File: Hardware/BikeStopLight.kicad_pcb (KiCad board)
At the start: 2 copper layers, 63 parts, among them J1 ST-Link, J2 PWR, J3 BAT, J4 Conn_01x01, J5 Conn_01x01, J6 Conn_01x08, Q1 NTD4909N, U1 MCP1703A-3302_SOT23, U2 STM32L052K8Tx, U3 RFM95W-868S2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

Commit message: WIP - Routed
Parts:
- removed J3: BAT, Connector_PinHeader_2.54mm:PinHeader_1x02_P2.54mm_Vertical
- added R8: 0 Ohm, Resistor_SMD:R_0805_2012Metric, F.Cu at (44.7, 169.4)
- BT1, BT2: moved to B.Cu
- moved J5 21.5 mm to (99.6, 164.6)
- moved C24 10.4 mm to (32.9, 161.0), turned to 0 degrees
- moved C7 8.23 mm to (65.8, 167.8), turned to 270 degrees
- moved Q1 1.84 mm to (56.9, 170.2)
- moved C27 1.36 mm to (107.7, 154.2)
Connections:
- C27 pad 2: VCC -> +3V3
- U3 pad 13: VCC -> +3V3
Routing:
- net VCC: track 9.09 -> 308.7 mm, vias 0 -> 18
- net +3V3: track 0.00 -> 122.4 mm, vias 0 -> 4
- net +BATT: track 0.00 -> 42.2 mm, vias 0 -> 1
- net /LDR_OUT: track 0.00 -> 33.5 mm, vias 0 -> 2
- net /LDR_PWR: track 0.00 -> 30.7 mm, vias 0 -> 2
- net Net-(D3-Pad2): track 0.00 -> 25.2 mm, vias 0 -> 2
- net GNDPWR: track 309.2 -> 288.1 mm
- net /NRST: track 21.5 -> 42.1 mm, vias 0 -> 4
- net Net-(D13-Pad2): track 0.00 -> 18.6 mm, vias 0 -> 2
- net /VBat_Scale: track 0.00 -> 16.7 mm
- net Net-(D4-Pad2): track 0.00 -> 14.6 mm, vias 0 -> 2
- net Net-(C19-Pad1): track 0.00 -> 9.04 mm
- net Net-(C20-Pad1): track 0.00 -> 7.94 mm
- net Net-(D12-Pad2): track 0.00 -> 7.87 mm
- net /LED_D5_DOUT: track 0.00 -> 7.68 mm
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
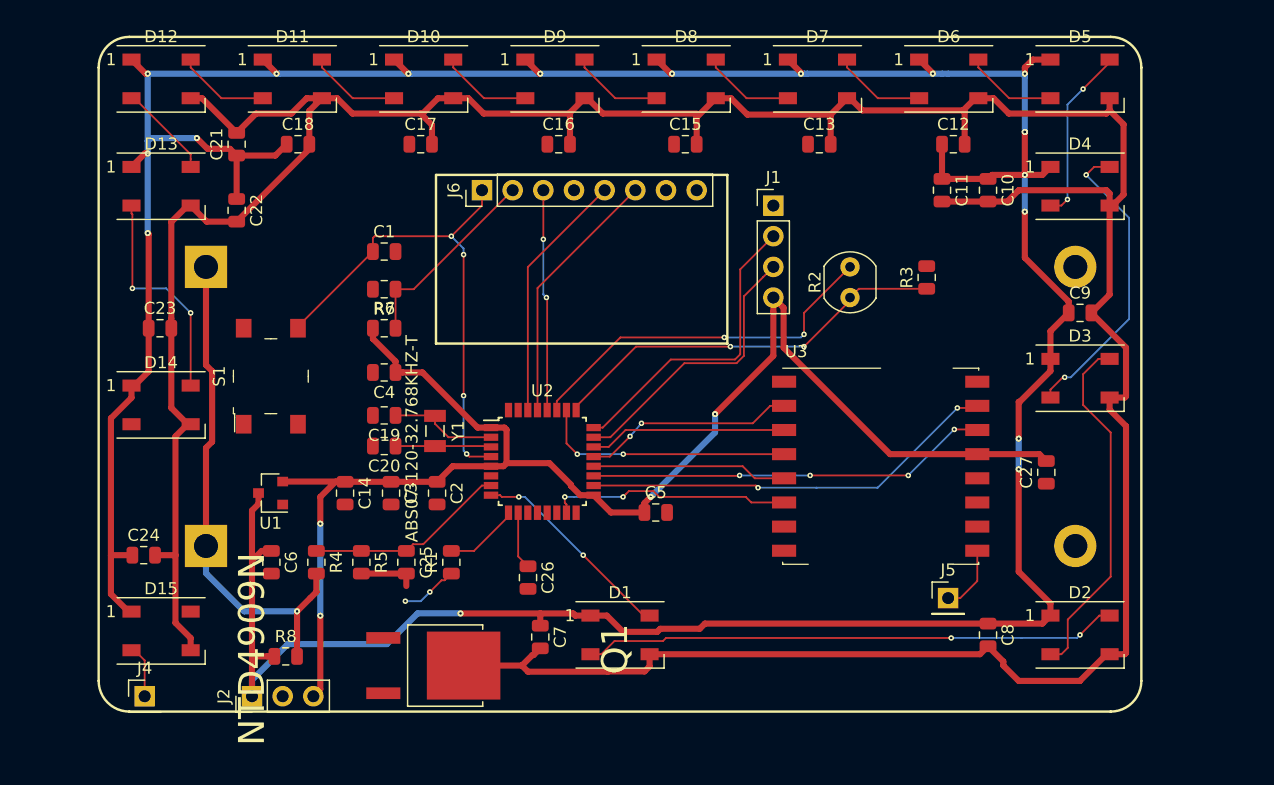
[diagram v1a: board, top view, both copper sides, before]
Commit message: WIP - Add touch & GND via
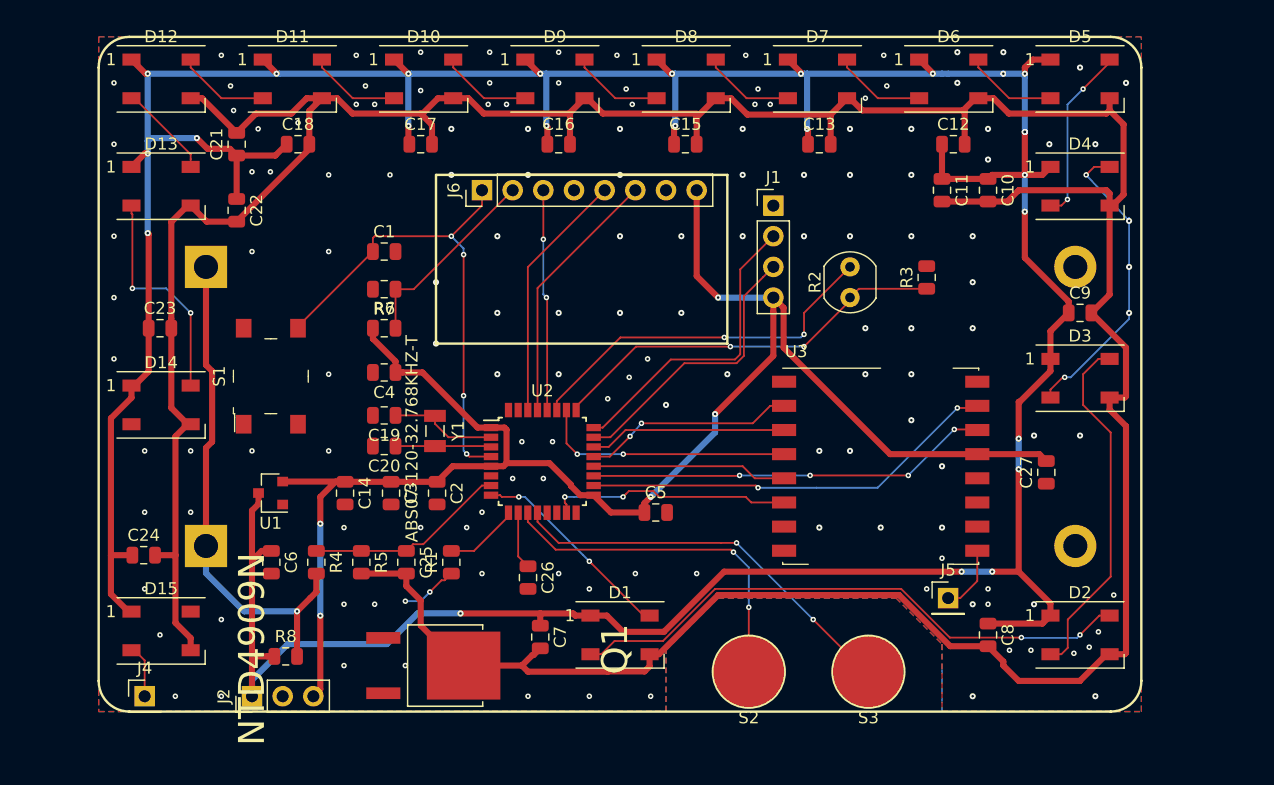
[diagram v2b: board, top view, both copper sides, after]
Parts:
- added S2: Touch_IO2, Perso:Capacitive_Touch_6_mm, F.Cu at (83.1, 170.7)
- added S3: Touch_IO3, Perso:Capacitive_Touch_6_mm, F.Cu at (93.0, 170.7)
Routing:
- net /TSC_G2_IO3: track 0.00 -> 33.3 mm, vias 0 -> 2
- net /TSC_G2_IO2: track 0.00 -> 29.3 mm, vias 0 -> 2
- net VCC: track 308.7 -> 336.5 mm, vias 18 -> 25
- net +3V3: track 122.4 -> 136.6 mm, vias 4 -> 5
- net GNDPWR: track 288.1 -> 300.3 mm
- net Net-(D1-Pad2): track 44.3 -> 47.6 mm
- net Net-(D3-Pad2): track 25.2 -> 25.7 mm, vias 2 -> 5
- net GND: vias 0 -> 134
- net (no net): vias 0 -> 8
- added copper zone on B.Cu, net GND
- added copper zone on F.Cu, net GND

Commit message: WIP - Add red light
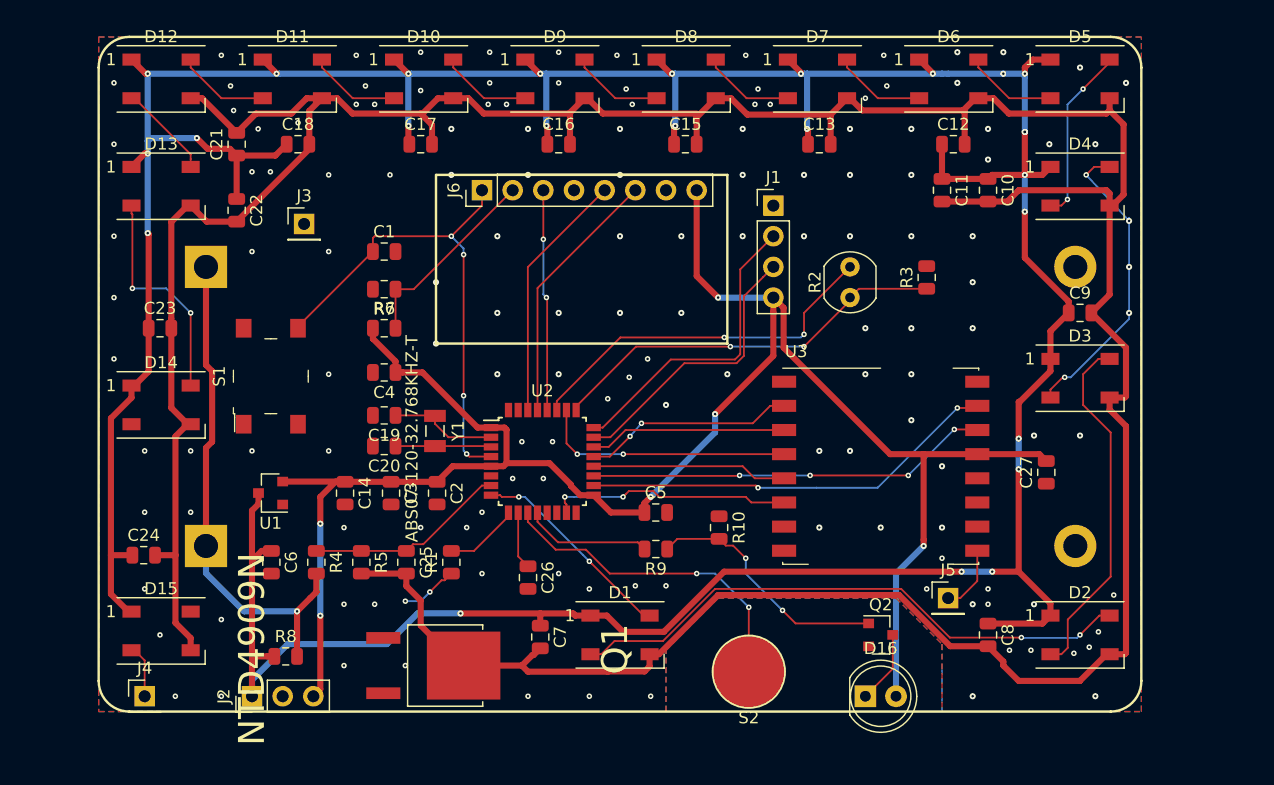
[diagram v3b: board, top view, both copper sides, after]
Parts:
- removed S3: Touch_IO3, Perso:Capacitive_Touch_6_mm
- added D16: LED, LED_THT:LED_D5.0mm, F.Cu at (92.7, 172.7)
- added J3: NRST, Connector_PinHeader_2.54mm:PinHeader_1x01_P2.54mm_Vertical, F.Cu at (46.2, 133.6)
- added Q2: BSS138, Package_TO_SOT_SMD:SOT-23, F.Cu at (94.0, 167.6)
- added R10: 100 kOhm, Resistor_SMD:R_0805_2012Metric, F.Cu at (80.6, 158.8)
- added R9: 160 Ohm, Resistor_SMD:R_0805_2012Metric, F.Cu at (75.4, 160.5)
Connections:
- U2 pad 12: /TSC_G2_IO3 -> /LED_DOWN
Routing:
- net /TSC_G2_IO3: track 33.3 -> 0.00 mm, vias 2 -> 0
- net +3V3: track 136.6 -> 157.6 mm, vias 5 -> 6
- net Net-(Q2-Pad1): track 0.00 -> 20.7 mm, vias 0 -> 2
- net /LED_DOWN: track 0.00 -> 10.6 mm
- net Net-(D16-Pad1): track 0.00 -> 6.02 mm
- net /TSC_G2_IO2: track 29.3 -> 27.3 mm

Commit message: Add reset connector
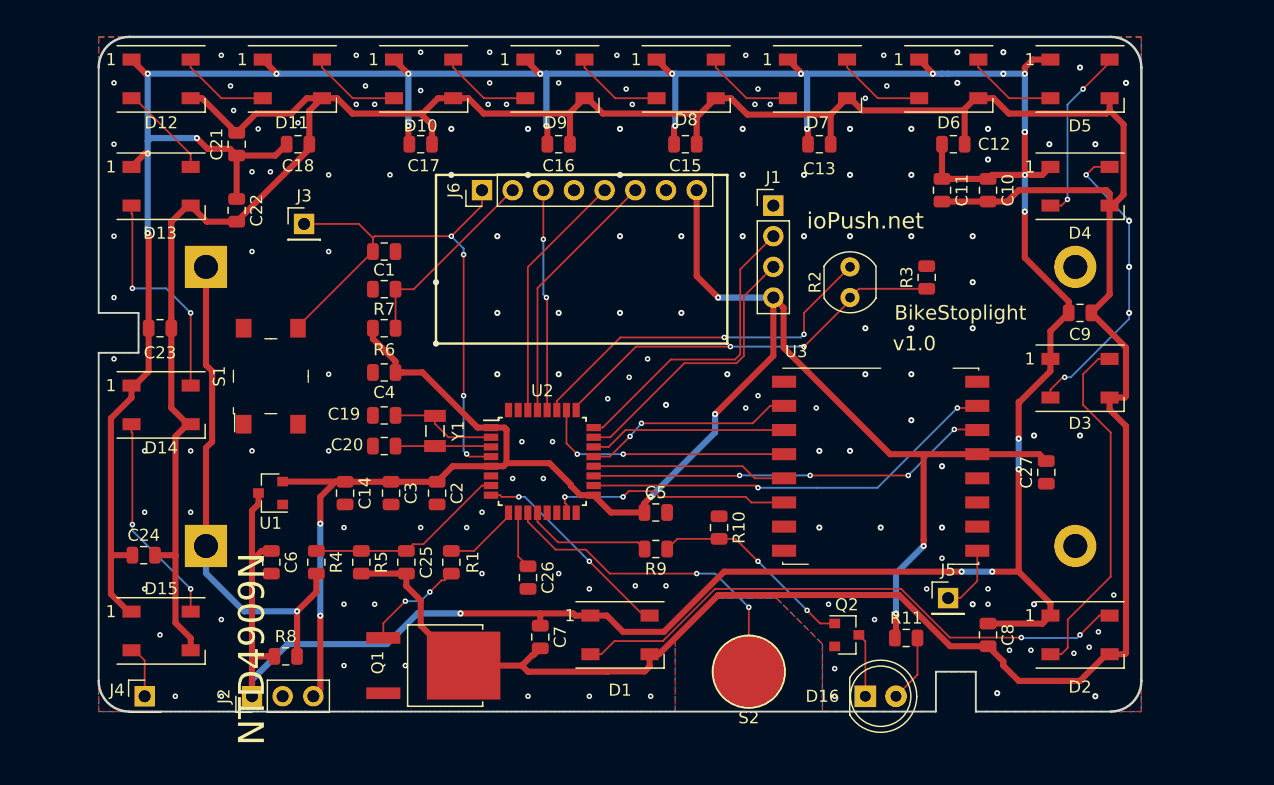
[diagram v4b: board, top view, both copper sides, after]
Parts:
- added R11: 165 Ohm, Resistor_SMD:R_0805_2012Metric, F.Cu at (96.1, 167.9)
- moved Q2 2.81 mm to (91.2, 167.6)
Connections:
- D16 pad 2: +3V3 -> Net-(D16-Pad2)
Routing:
- net Net-(D14-Pad2): track 0.00 -> 17.5 mm, vias 0 -> 2
- net /NRST: track 42.1 -> 48.3 mm
- net Net-(D16-Pad2): track 0.00 -> 5.56 mm
- net +3V3: track 157.6 -> 152.8 mm, vias 6 -> 7
- net Net-(Q1-Pad1): track 4.76 -> 8.56 mm
- net Net-(Q2-Pad1): track 20.7 -> 17.1 mm
- net Net-(D16-Pad1): track 6.02 -> 5.30 mm
- net GND: vias 134 -> 147
- net (no net): vias 8 -> 2
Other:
- board outline added: 86.4 x 55.9 mm
- board text added: "BikeStoplight"
- board text added: "ioPush.net"
- board text added: "v1.0"

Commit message: Change fixing holes, silkscreen changes
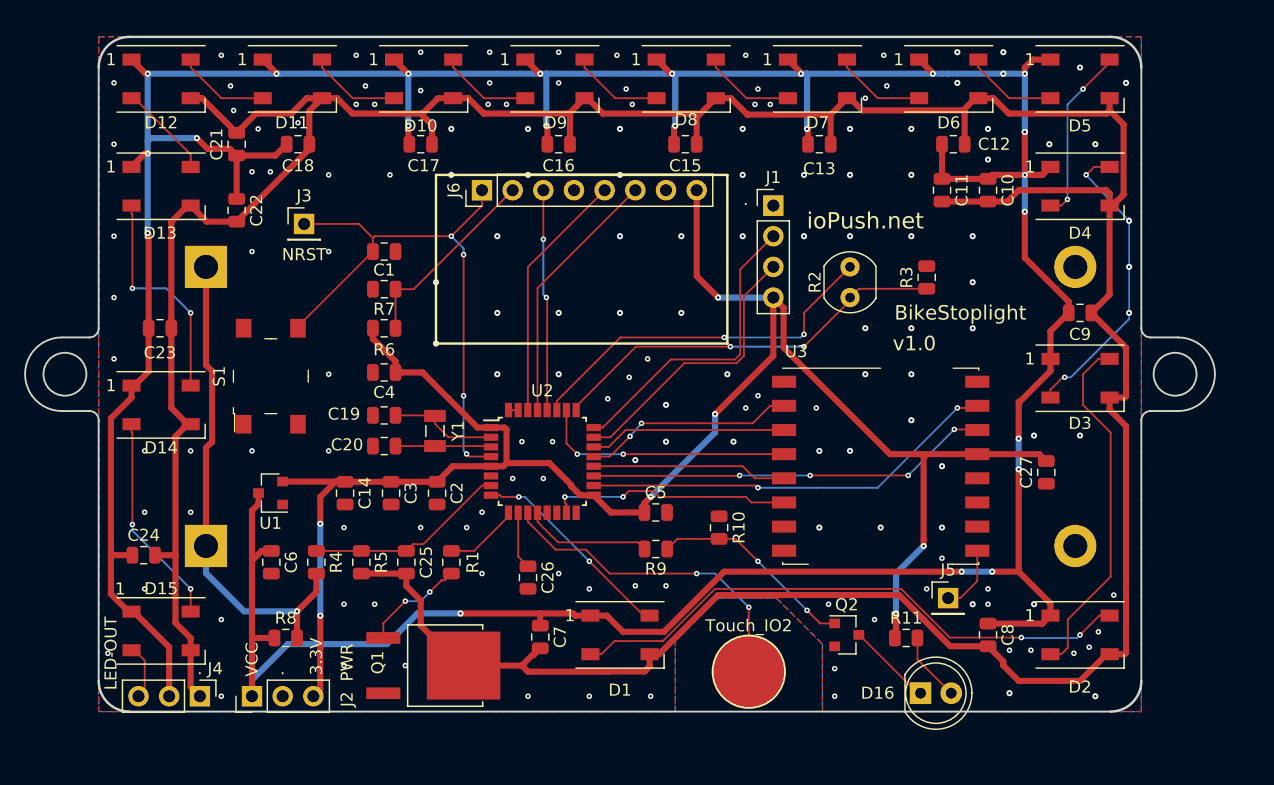
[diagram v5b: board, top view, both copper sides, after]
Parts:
- J4: value Conn_01x01 -> LED-OUT; footprint Connector_PinHeader_2.54mm:PinHeader_1x01_P2.54mm_Vertical -> Connector_PinHeader_2.54mm:PinHeader_1x03_P2.54mm_Vertical
- moved D16 4.58 mm to (97.3, 172.5)
- moved J4 4.57 mm to (37.6, 172.7), turned to 270 degrees
- moved R8 1.52 mm to (44.7, 167.9)
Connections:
- J4 pad 1: Net-(D15-Pad2) -> GNDPWR
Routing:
- net VCC: track 336.5 -> 344.9 mm
- net GNDPWR: track 300.3 -> 304.4 mm
- net Net-(D16-Pad1): track 5.30 -> 7.56 mm
- net +BATT: track 42.2 -> 40.6 mm
- net GND: track 0.00 -> 0.80 mm, vias 147 -> 151
- net (no net): vias 2 -> 0
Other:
- board size 86.4 x 55.9 mm -> 98.6 x 55.9 mm
- board text added: "."
- board text added: "3.3V"
- board text added: "NRST"
- board text added: "VCC"

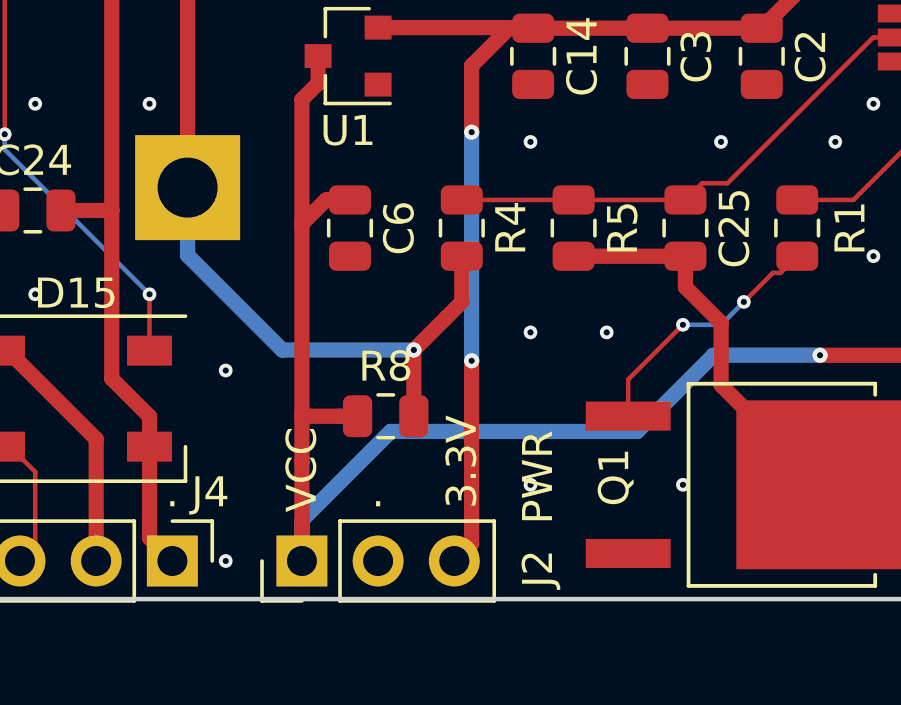
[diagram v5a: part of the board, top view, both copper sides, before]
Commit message: Add connector for Vbat to Vcc
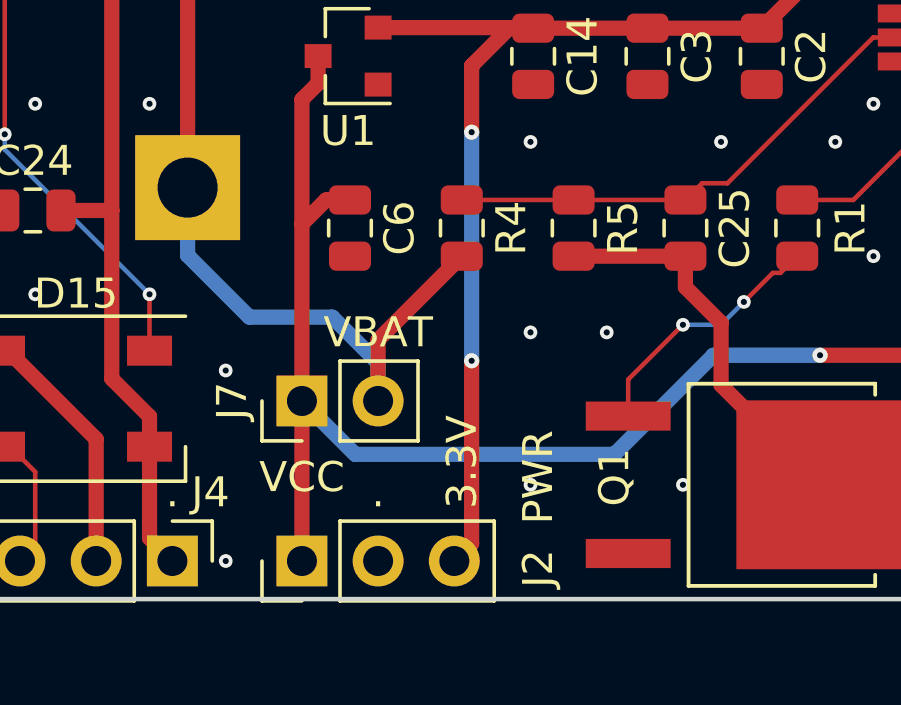
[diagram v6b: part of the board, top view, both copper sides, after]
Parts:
- removed R8: 0 Ohm, Resistor_SMD:R_0805_2012Metric
- added J7: VCC_VBAT, Connector_PinHeader_2.54mm:PinHeader_1x02_P2.54mm_Vertical, F.Cu at (41.9, 167.4)
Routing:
- net VCC: track 344.9 -> 341.5 mm
- net +BATT: track 40.6 -> 40.9 mm, vias 1 -> 0
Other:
- board text added: "VBAT"

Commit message: Add JLPCB prod text placeholder
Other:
- board text added: "JLCJLCJLCJLC"
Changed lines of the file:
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@@
   (general
     (thickness 1.6)
-    (drawings 36)
+    (drawings 37)
     (tracks 768)
     (zones 0)
@@
       (creategerberjobfile false)
       (excludeedgelayer true)
-      (linewidth 0.100000)
+      (linewidth 0.150000)
       (plotframeref false)
       (viasonmask false)
       (mode 1)
-      (useauxorigin false)
+      (useauxorigin true)
       (hpglpennumber 1)
       (hpglpenspeed 20)
@@
       (outputformat 1)
       (mirror false)
-      (drillshape 1)
+      (drillshape 0)
       (scaleselection 1)
-      (outputdirectory ""))
+      (outputdirectory "Gerbers/"))
   )
   (net 0 "")
@@
       (net 1 "Net-(S1-Pad1)"))
   )
+  (gr_text JLCJLCJLCJLC (at 69.342 137.922) (layer F.SilkS)
+    (effects (font (size 1.2 1.2) (thickness 0.1)))
+  )
   (gr_text VBAT (at 44.45 165.1) (layer F.SilkS)
